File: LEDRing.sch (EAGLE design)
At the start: 11 parts, among them U1 ATMEGA328P-AU, Y1 16MHZ

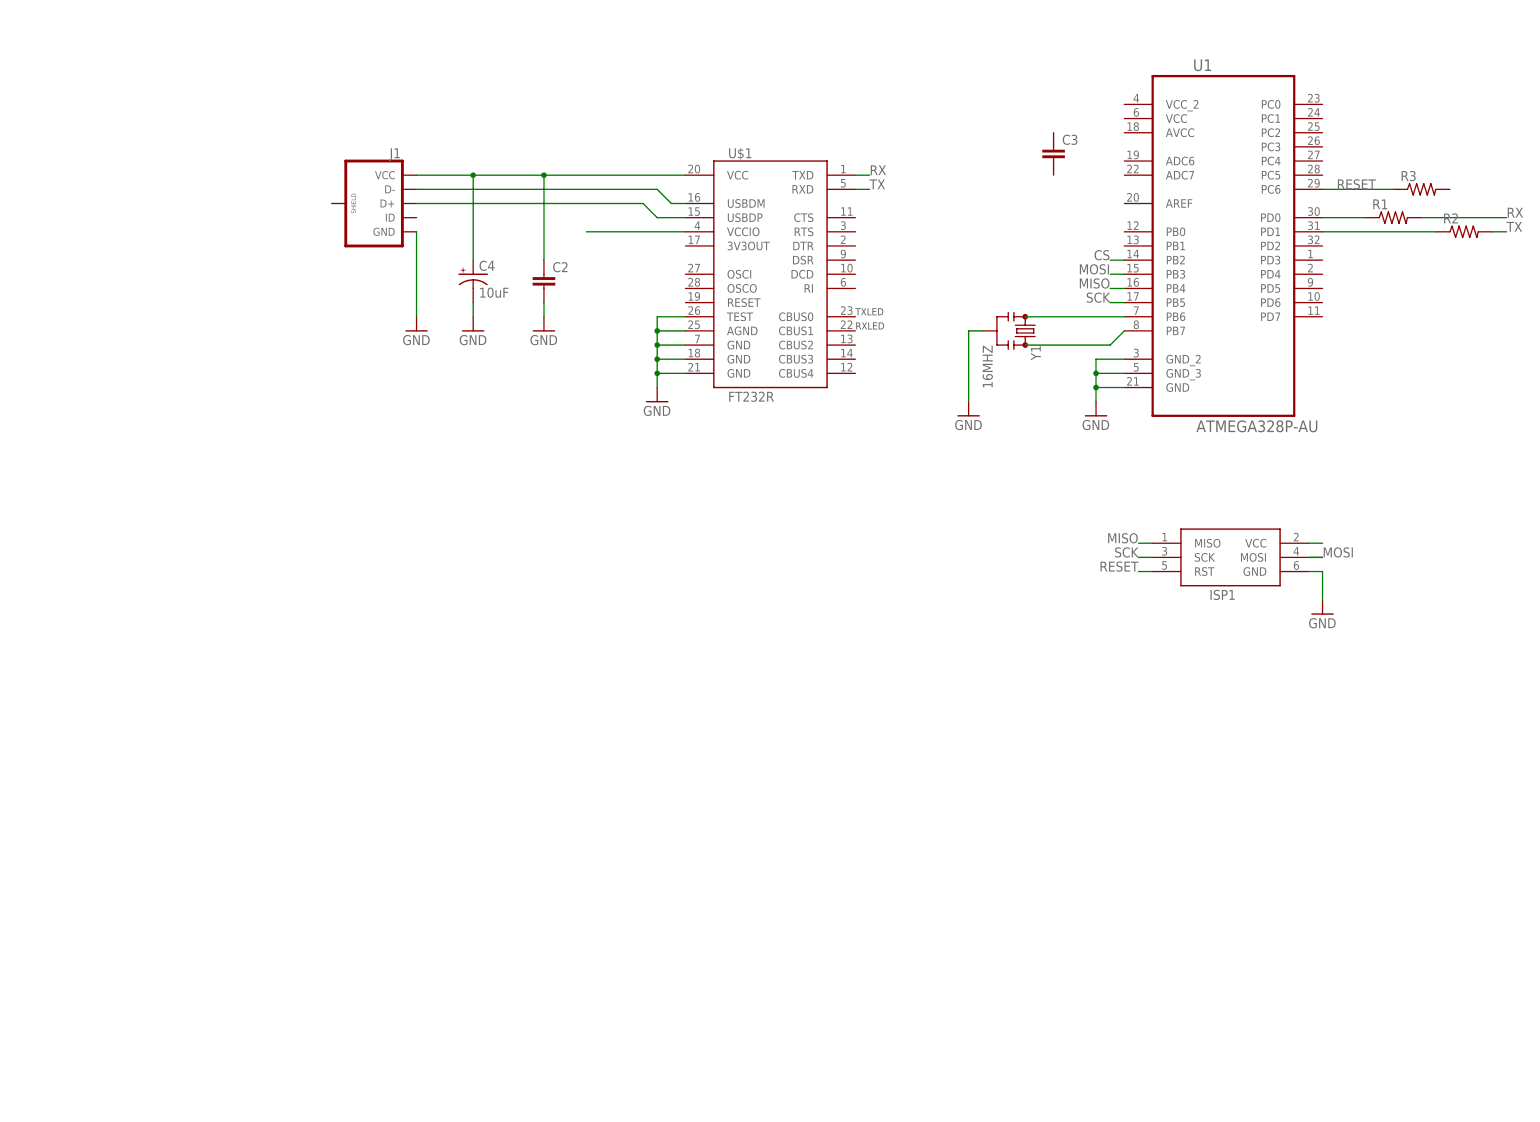
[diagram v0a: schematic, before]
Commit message: Added accelerometer Added power Added LEDs
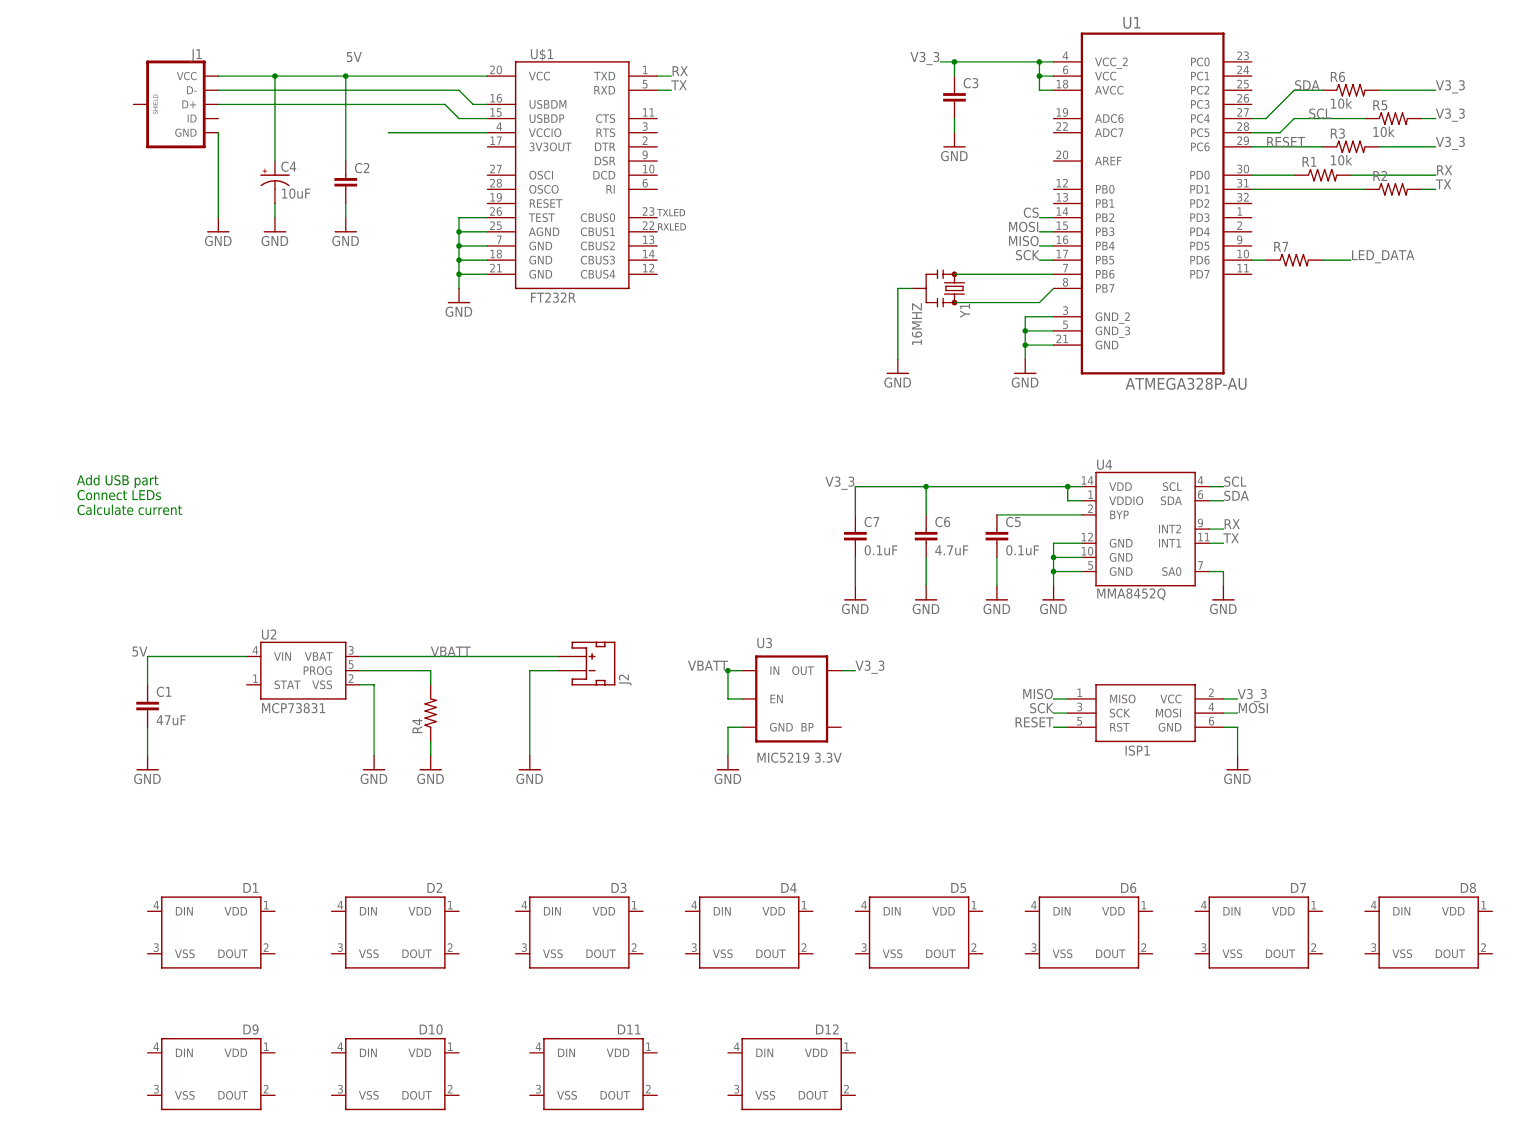
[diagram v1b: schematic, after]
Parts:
- added C1: 47uF, SparkFun-Capacitors:CAP0603-CAP
- added C5, C7: 0.1uF, SparkFun-Capacitors:CAP0603-CAP
- added C6: 4.7uF, SparkFun-Capacitors:CAP0603-CAP
- added D1, D10, D11, D12, D2, D3, D4, D5, D6, D7, D8, D9: (no value), SparkFun-LED:WS2812B
- added J2: (no value), SparkFun-Connectors:JST_2MM_MALE
- added R4, R7: (no value), SparkFun-Passives:RESISTOR0603-RES
- added R5, R6: 10k, SparkFun-Passives:RESISTOR0603-RES
- added U2: MCP73831, SparkFun-PowerIC:MCP73831
- added U3: MIC5219 3.3V, SparkFun-PowerIC:V_REG_MIC52193.3V
- added U4: MMA8452Q, SparkFun-Sensors:MMA8452Q
- R3: value (none) -> 10k
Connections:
- removed net N$12: ISP1.VCC
- new net 5V: C1.1, C2.1, C4.+, J1.VCC, U$1.VCC, U2.VIN
- new net LED_DATA: R7.2
- new net N$10: R7.1, U1.PD6
- new net N$9: R4.2, U2.PROG
- new net SCL: R5.1, U1.PC5, U4.SCL
- new net SDA: R6.1, U1.PC4, U4.SDA
- new net V3_3: C3.1, C6.1, C7.1, ISP1.VCC, R3.2, R5.2, R6.2, U1.AVCC, U1.VCC, U1.VCC_2, U3.OUT, U4.VDD, U4.VDDIO
- new net VBATT: J2.+, U2.VBAT, U3.EN, U3.IN
- net GND: now also C1.2, C3.2, C5.2, C6.2, C7.2, J2.-, R4.1, U2.VSS, U3.GND, U4.GND@0, U4.GND@1, U4.GND@2, U4.SA0
- net N$3: now also C5.1, U4.BYP; no longer C2.1, C4.+, J1.VCC, U$1.VCC
- net RX: now also U4.INT2
- net TX: now also U4.INT1
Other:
- note added: "Add USB part Connect LEDs Calculate current"
- moved on the sheet: C2, C3, C4, ISP1, J1, R1, R2, R3, U$1, U1, Y1

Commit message: More updates to layout
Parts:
- removed J2: (no value), SparkFun-Connectors:JST_2MM_MALE
- added J3: (no value), SparkFun-Connectors:M02PTH
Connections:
- new net LED_CONT: D6.DOUT, D7.VSS
- new net N$14: D1.VDD
- new net N$15: D1.DOUT, D2.DIN
- new net N$16: D2.DOUT, D3.DIN
- new net N$17: D3.DOUT, D4.DIN
- new net N$18: D4.DOUT, D5.DIN
- new net N$19: D5.DOUT, D6.DIN
- new net N$20: D7.DOUT, D8.DIN
- new net N$21: D8.DOUT, D9.DIN
- new net N$22: D10.DIN, D9.DOUT
- new net N$23: D10.DOUT, D11.DIN
- new net N$24: D11.DOUT, D12.DIN
- net GND: now also J3.2; no longer J2.-
- net VBATT: now also J3.1; no longer J2.+
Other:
- moved on the sheet: D10, D11, D12, D4, D5, D6, D7, D8, D9
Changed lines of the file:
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@@
 <?xml version="1.0" encoding="utf-8"?>
 <!DOCTYPE eagle SYSTEM "eagle.dtd">
-<eagle version="7.7.0">
+<eagle version="7.3.0">
 <drawing>
 <settings>
@@
 <part name="GND9" library="SparkFun-Aesthetics" deviceset="GND" device=""/>
 <part name="GND10" library="SparkFun-Aesthetics" deviceset="GND" device=""/>
-<part name="J2" library="SparkFun-Connectors" deviceset="JST_2MM_MALE" device=""/>
 <part name="GND11" library="SparkFun-Aesthetics" deviceset="GND" device=""/>
 <part name="U3" library="SparkFun-PowerIC" deviceset="V_REG_MIC5219" device="3.3V" value="MIC5219 3.3V"/>
@@
 <part name="D11" library="SparkFun-LED" deviceset="WS2812B" device=""/>
 <part name="D12" library="SparkFun-LED" deviceset="WS2812B" device=""/>
+<part name="J3" library="SparkFun-Connectors" deviceset="M02" device="PTH"/>
 </parts>
 <sheets>
@@
 <instance part="GND9" gate="1" x="-35.56" y="-30.48"/>
 <instance part="GND10" gate="1" x="-45.72" y="-30.48"/>
-<instance part="J2" gate="G$1" x="-7.62" y="-12.7" rot="MR90"/>
 <instance part="GND11" gate="1" x="-17.78" y="-30.48"/>
 <instance part="U3" gate="G$1" x="30.48" y="-17.78"/>
@@
 <instance part="D2" gate="G$1" x="-35.56" y="-60.96" rot="MR0"/>
 <instance part="D3" gate="G$1" x="-2.54" y="-60.96" rot="MR0"/>
-<instance part="D4" gate="G$1" x="27.94" y="-60.96" rot="MR0"/>
+<instance part="D4" gate="G$1" x="30.48" y="-60.96" rot="MR0"/>
 <instance part="R7" gate="G$1" x="119.38" y="60.96"/>
-<instance part="D5" gate="G$1" x="58.42" y="-60.96" rot="MR0"/>
-<instance part="D6" gate="G$1" x="88.9" y="-60.96" rot="MR0"/>
-<instance part="D7" gate="G$1" x="119.38" y="-60.96" rot="MR0"/>
-<instance part="D8" gate="G$1" x="149.86" y="-60.96" rot="MR0"/>
-<instance part="D9" gate="G$1" x="-68.58" y="-86.36" rot="MR0"/>
-<instance part="D10" gate="G$1" x="-35.56" y="-86.36" rot="MR0"/>
-<instance part="D11" gate="G$1" x="0" y="-86.36" rot="MR0"/>
-<instance part="D12" gate="G$1" x="35.56" y="-86.36" rot="MR0"/>
+<instance part="D5" gate="G$1" x="63.5" y="-60.96" rot="MR0"/>
+<instance part="D6" gate="G$1" x="99.06" y="-60.96" rot="MR0"/>
+<instance part="D7" gate="G$1" x="-68.58" y="-83.82" rot="MR0"/>
+<instance part="D8" gate="G$1" x="-35.56" y="-83.82" rot="MR0"/>
+<instance part="D9" gate="G$1" x="-2.54" y="-83.82" rot="MR0"/>
+<instance part="D10" gate="G$1" x="30.48" y="-83.82" rot="MR0"/>
+<instance part="D11" gate="G$1" x="63.5" y="-83.82" rot="MR0"/>
+<instance part="D12" gate="G$1" x="99.06" y="-83.82" rot="MR0"/>
+<instance part="J3" gate="G$1" x="-2.54" y="-10.16" rot="R180"/>
 </instances>
 <busses>
@@
 </segment>
 <segment>
-<pinref part="J2" gate="G$1" pin="-"/>
-<wire x1="-12.7" y1="-12.7" x2="-17.78" y2="-12.7" width="0.1524" layer="91"/>
+<wire x1="-10.16" y1="-12.7" x2="-17.78" y2="-12.7" width="0.1524" layer="91"/>
 <wire x1="-17.78" y1="-12.7" x2="-17.78" y2="-27.94" width="0.1524" layer="91"/>
 <pinref part="GND11" gate="1" pin="GND"/>
+<pinref part="J3" gate="G$1" pin="2"/>
 </segment>
 <segment>
@@
 <pinref part="U2" gate="G$1" pin="VBAT"/>
 <label x="-35.56" y="-10.16" size="1.778" layer="95"/>
-<pinref part="J2" gate="G$1" pin="+"/>
-<wire x1="-12.7" y1="-10.16" x2="-48.26" y2="-10.16" width="0.1524" layer="91"/>
+<wire x1="-10.16" y1="-10.16" x2="-48.26" y2="-10.16" width="0.1524" layer="91"/>
+<pinref part="J3" gate="G$1" pin="1"/>
 </segment>
 <segment>
@@
 </segment>
 </net>
+<net name="N$14" class="0">
+<segment>
+<pinref part="D1" gate="G$1" pin="VDD"/>
+<wire x1="-63.5" y1="-55.88" x2="-60.96" y2="-55.88" width="0.1524" layer="91"/>
+</segment>
+</net>
+<net name="N$15" class="0">
+<segment>
+<pinref part="D1" gate="G$1" pin="DOUT"/>
+<pinref part="D2" gate="G$1" pin="DIN"/>
+<wire x1="-63.5" y1="-63.5" x2="-55.88" y2="-55.88" width="0.1524" layer="91"/>
+<wire x1="-55.88" y1="-55.88" x2="-53.34" y2="-55.88" width="0.1524" layer="91"/>
+</segment>
+</net>
+<net name="N$16" class="0">
+<segment>
+<pinref part="D2" gate="G$1" pin="DOUT"/>
+<pinref part="D3" gate="G$1" pin="DIN"/>
+<wire x1="-30.48" y1="-63.5" x2="-22.86" y2="-55.88" width="0.1524" layer="91"/>
+<wire x1="-22.86" y1="-55.88" x2="-20.32" y2="-55.88" width="0.1524" layer="91"/>
+</segment>
+</net>
+<net name="N$17" class="0">
+<segment>
+<pinref part="D3" gate="G$1" pin="DOUT"/>
+<pinref part="D4" gate="G$1" pin="DIN"/>
+<wire x1="2.54" y1="-63.5" x2="10.16" y2="-55.88" width="0.1524" layer="91"/>
+<wire x1="10.16" y1="-55.88" x2="12.7" y2="-55.88" width="0.1524" layer="91"/>
+</segment>
+</net>
+<net name="N$18" class="0">
+<segment>
+<pinref part="D4" gate="G$1" pin="DOUT"/>
+<pinref part="D5" gate="G$1" pin="DIN"/>
+<wire x1="35.56" y1="-63.5" x2="43.18" y2="-55.88" width="0.1524" layer="91"/>
+<wire x1="43.18" y1="-55.88" x2="45.72" y2="-55.88" width="0.1524" layer="91"/>
+</segment>
+</net>
+<net name="N$19" class="0">
+<segment>
+<pinref part="D5" gate="G$1" pin="DOUT"/>
+<pinref part="D6" gate="G$1" pin="DIN"/>
+<wire x1="68.58" y1="-63.5" x2="78.74" y2="-55.88" width="0.1524" layer="91"/>
+<wire x1="78.74" y1="-55.88" x2="81.28" y2="-55.88" width="0.1524" layer="91"/>
+</segment>
+</net>
+<net name="LED_CONT" class="0">
+<segment>
+<pinref part="D6" gate="G$1" pin="DOUT"/>
+<wire x1="104.14" y1="-63.5" x2="111.76" y2="-63.5" width="0.1524" layer="91"/>
+<label x="106.68" y="-63.5" size="1.778" layer="95"/>
+</segment>
+<segment>
+<pinref part="D7" gate="G$1" pin="VSS"/>
+<wire x1="-86.36" y1="-86.36" x2="-91.44" y2="-86.36" width="0.1524" layer="91"/>
+<label x="-91.44" y="-86.36" size="1.778" layer="95" rot="MR0"/>
+</segment>
+</net>
+<net name="N$20" class="0">
+<segment>
+<pinref part="D7" gate="G$1" pin="DOUT"/>
+<pinref part="D8" gate="G$1" pin="DIN"/>
+<wire x1="-63.5" y1="-86.36" x2="-55.88" y2="-78.74" width="0.1524" layer="91"/>
+<wire x1="-55.88" y1="-78.74" x2="-53.34" y2="-78.74" width="0.1524" layer="91"/>
+</segment>
+</net>
+<net name="N$21" class="0">
+<segment>
+<pinref part="D8" gate="G$1" pin="DOUT"/>
+<pinref part="D9" gate="G$1" pin="DIN"/>
+<wire x1="-30.48" y1="-86.36" x2="-22.86" y2="-78.74" width="0.1524" layer="91"/>
+<wire x1="-22.86" y1="-78.74" x2="-20.32" y2="-78.74" width="0.1524" layer="91"/>
+</segment>
+</net>
+<net name="N$22" class="0">
+<segment>
+<pinref part="D9" gate="G$1" pin="DOUT"/>
+<pinref part="D10" gate="G$1" pin="DIN"/>
+<wire x1="2.54" y1="-86.36" x2="10.16" y2="-78.74" width="0.1524" layer="91"/>
+<wire x1="10.16" y1="-78.74" x2="12.7" y2="-78.74" width="0.1524" layer="91"/>
+</segment>
+</net>
+<net name="N$23" class="0">
+<segment>
+<pinref part="D10" gate="G$1" pin="DOUT"/>
+<pinref part="D11" gate="G$1" pin="DIN"/>
+<wire x1="35.56" y1="-86.36" x2="43.18" y2="-78.74" width="0.1524" layer="91"/>
+<wire x1="43.18" y1="-78.74" x2="45.72" y2="-78.74" width="0.1524" layer="91"/>
+</segment>
+</net>
+<net name="N$24" class="0">
+<segment>
+<pinref part="D11" gate="G$1" pin="DOUT"/>
+<pinref part="D12" gate="G$1" pin="DIN"/>
+<wire x1="68.58" y1="-86.36" x2="76.2" y2="-78.74" width="0.1524" layer="91"/>
+<wire x1="76.2" y1="-78.74" x2="81.28" y2="-78.74" width="0.1524" layer="91"/>
+</segment>
+</net>

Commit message: Updated schematics
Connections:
- removed net N$14: D1.VDD
- net VBATT: now also D1.VDD, D2.VDD, D3.VDD, D4.VDD, D5.VDD, D6.VDD
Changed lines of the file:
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@@
 <junction x="17.78" y="-12.7"/>
+</segment>
+<segment>
+<pinref part="D1" gate="G$1" pin="VDD"/>
+<wire x1="-63.5" y1="-55.88" x2="-60.96" y2="-53.34" width="0.1524" layer="91"/>
+</segment>
+<segment>
+<pinref part="D2" gate="G$1" pin="VDD"/>
+<wire x1="-30.48" y1="-55.88" x2="-27.94" y2="-53.34" width="0.1524" layer="91"/>
+<label x="-27.94" y="-53.34" size="1.778" layer="95"/>
+</segment>
+<segment>
+<pinref part="D3" gate="G$1" pin="VDD"/>
+<wire x1="2.54" y1="-55.88" x2="5.08" y2="-53.34" width="0.1524" layer="91"/>
+<label x="5.08" y="-53.34" size="1.778" layer="95"/>
+</segment>
+<segment>
+<pinref part="D4" gate="G$1" pin="VDD"/>
+<wire x1="35.56" y1="-55.88" x2="38.1" y2="-53.34" width="0.1524" layer="91"/>
+<label x="38.1" y="-53.34" size="1.778" layer="95"/>
+</segment>
+<segment>
+<pinref part="D5" gate="G$1" pin="VDD"/>
+<wire x1="68.58" y1="-55.88" x2="71.12" y2="-53.34" width="0.1524" layer="91"/>
+<label x="71.12" y="-53.34" size="1.778" layer="95"/>
+</segment>
+<segment>
+<pinref part="D6" gate="G$1" pin="VDD"/>
+<wire x1="104.14" y1="-55.88" x2="106.68" y2="-53.34" width="0.1524" layer="91"/>
+<label x="106.68" y="-53.34" size="1.778" layer="95"/>
 </segment>
 </net>
@@
 </segment>
 </net>
-<net name="N$14" class="0">
-<segment>
-<pinref part="D1" gate="G$1" pin="VDD"/>
-<wire x1="-63.5" y1="-55.88" x2="-60.96" y2="-55.88" width="0.1524" layer="91"/>
-</segment>
-</net>
